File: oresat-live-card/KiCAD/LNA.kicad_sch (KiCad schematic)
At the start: 33 parts, among them J12 U.FL, J14 Conn_01x02, U18 TQP3M9037, U27 PAT1220-C-3DB, U28 PD2328J5050S2HF, U29 LTC5538

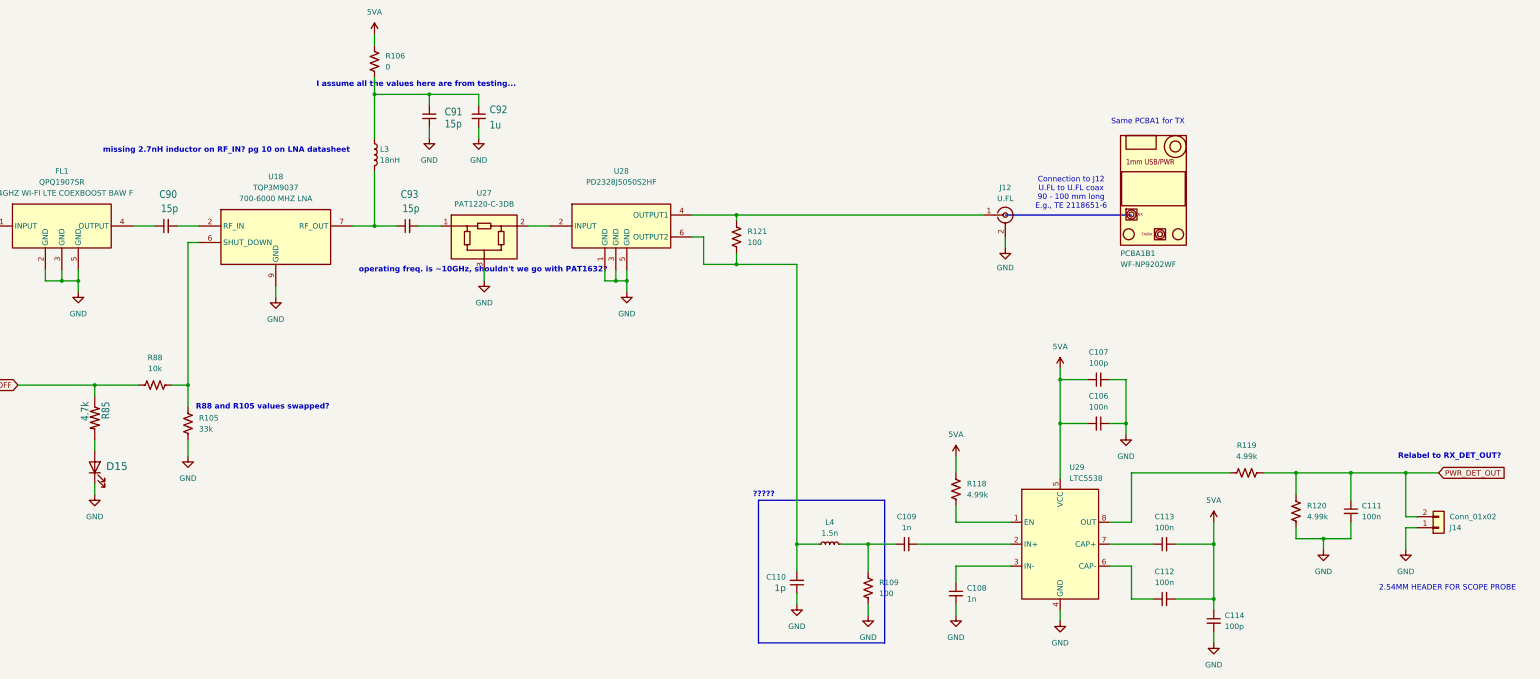
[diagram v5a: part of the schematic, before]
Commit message: swapped placement of R105 and R88, changed R109 from 100 to 56 ohms, relabelled PWR_DET_OUT to RX_DET_OUT, added inverter to TX/RX Control switch and swapped RF1 and RF2
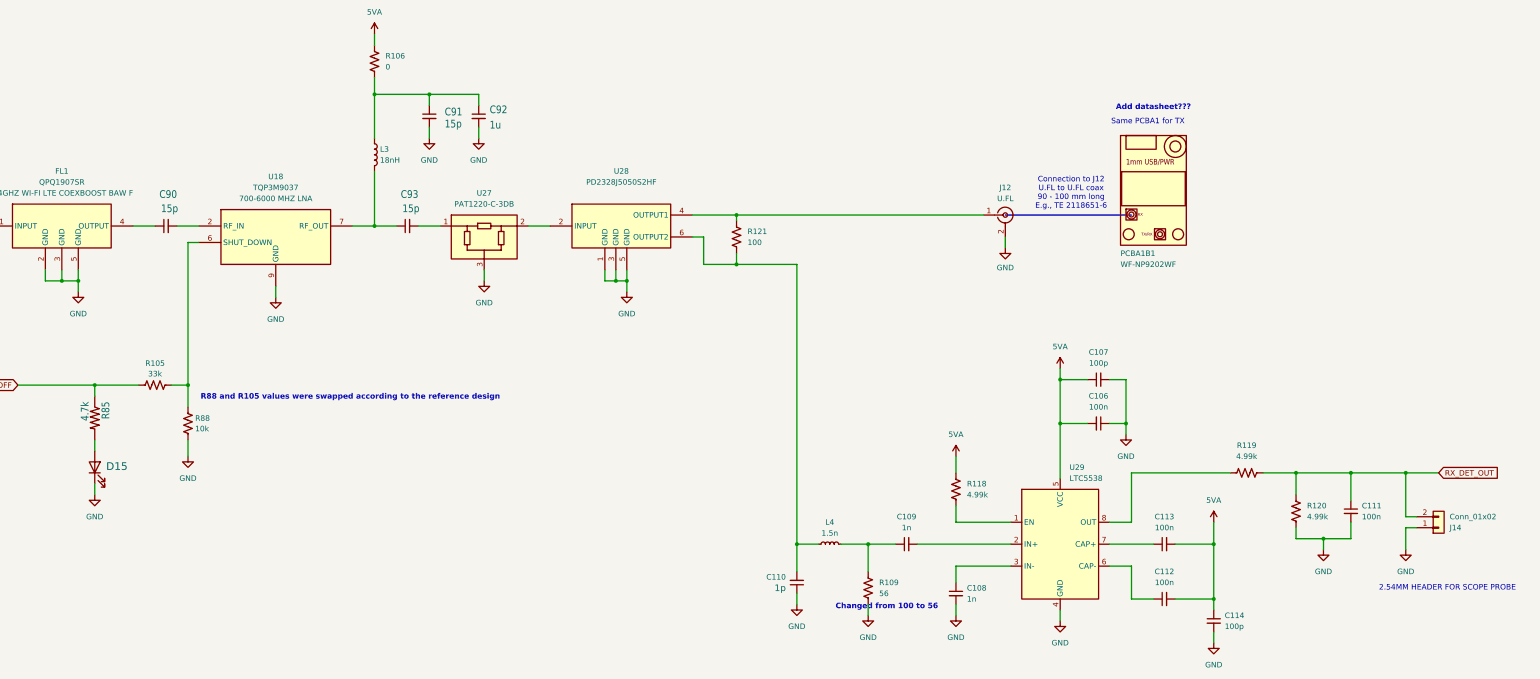
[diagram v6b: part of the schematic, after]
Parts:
- R109: value 100 -> 56
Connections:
- net GND: now also R88.2; no longer R105.2
- net PA_ON_LNA_OFF: now also R105.1; no longer R88.2
- net at R88.1, U18.6 (SHUT_DOWN): now also R105.2; no longer R105.1
- net PWR_DET_OUT renamed RX_DET_OUT
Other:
- note added: "Add datasheet???"
- note added: "Changed from 100 to 56"
- note added: "R88 and R105 values were swapped according to the reference design"
- note removed: "?????"
- note removed: "I assume all the values here are from testing..."
- note removed: "R88 and R105 values swapped?"
- note removed: "Relabel to RX_DET_OUT?"
- note removed: "missing 2.7nH inductor on RF_IN? pg 10 on LNA datasheet"
- note removed: "operating freq. is ~10GHz, shouldn't we go with PAT1632?"
- moved on the sheet: R105, R88
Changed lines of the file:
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@@
 		(rev "2")
 	)
-	(rectangle
-		(start 237.49 139.7)
-		(end 266.7 172.72)
-		(stroke
-			(width 0)
-			(type default)
-		)
-		(fill
-			(type none)
-		)
-	)
-	(text "I assume all the values here are from testing..."
-		(exclude_from_sim no)
-		(at 158.242 43.434 0)
-		(effects
-			(font
-				(size 1.27 1.27)
-				(thickness 0.254)
-				(bold yes)
-			)
-		)
-	)
 	(text "Same PCBA1 for TX"
 		(exclude_from_sim no)
@@
 		)
 	)
-	(text "missing 2.7nH inductor on RF_IN? pg 10 on LNA datasheet"
+	(text "Add datasheet??? "
 		(exclude_from_sim no)
-		(at 114.3 58.674 0)
-		(effects
-			(font
-				(size 1.27 1.27)
-				(thickness 0.254)
-				(bold yes)
-			)
-		)
-	)
-	(text "operating freq. is ~10GHz, shouldn't we go with PAT1632?"
-		(exclude_from_sim no)
-		(at 173.736 86.36 0)
+		(at 328.93 48.768 0)
 		(effects
 			(font
@@
 		)
 	)
-	(text "?????"
+	(text "Changed from 100 to 56"
 		(exclude_from_sim no)
-		(at 238.7267 138.3976 0)
+		(at 267.208 164.338 0)
 		(effects
 			(font
@@
 		)
 	)
-	(text "R88 and R105 values swapped?"
+	(text "R88 and R105 values were swapped according to the reference design"
 		(exclude_from_sim no)
-		(at 122.682 118.11 0)
-		(effects
-			(font
-				(size 1.27 1.27)
-				(thickness 0.254)
-				(bold yes)
-			)
-		)
-	)
-	(text "Relabel to RX_DET_OUT?"
-		(exclude_from_sim no)
-		(at 397.51 129.54 0)
+		(at 143.002 115.824 0)
 		(effects
 			(font
@@
 		)
 	)
-	(global_label "PWR_DET_OUT"
+	(global_label "RX_DET_OUT"
 		(shape input)
 		(at 394.97 133.35 0)
@@
 		)
 		(property "Intersheetrefs" "${INTERSHEET_REFS}"
-			(at 410.897 133.35 0)
+			(at 409.3851 133.35 0)
 			(effects
 				(font
@@
 			)
 		)
-		(property "Value" "100"
+		(property "Value" "56"
 			(at 265.43 161.2899 0)
 			(effects
@@
 	(symbol
 		(lib_id "Device:R_US")
-		(at 105.41 121.92 0)
+		(at 97.79 113.03 90)
 		(unit 1)
 		(exclude_from_sim no)
@@
 		(fields_autoplaced yes)
 		(property "Reference" "R105"
-			(at 107.95 120.6499 0)
+			(at 97.79 107.9965 90)
 			(effects
 				(font
 					(size 1.27 1.27)
 				)
-				(justify left)
 			)
 		)
 		(property "Value" "33k"
-			(at 107.95 123.1899 0)
+			(at 97.79 110.4208 90)
 			(effects
 				(font
 					(size 1.27 1.27)
 				)
-				(justify left)
 			)
 		)
 		(property "Footprint" "Resistor_SMD:R_0603_1608Metric"
-			(at 106.426 122.174 90)
+			(at 98.044 112.014 90)
 			(effects
 				(font
@@
 		)
 		(property "Datasheet" "~"
-			(at 105.41 121.92 0)
+			(at 97.79 113.03 0)
 			(effects
 				(font
@@
 		)
 		(property "Description" "RES 33K OHM 1% 1/10W 0603"
-			(at 105.41 121.92 0)
+			(at 97.79 113.03 0)
 			(effects
 				(font
@@
 		)
 		(property "DPN" "10-ERJ-U03F3302VCT-ND "
-			(at 105.41 121.92 0)
+			(at 97.79 113.03 0)
 			(effects
 				(font
@@
 		)
 		(property "Distributor" "DigiKey"
-			(at 105.41 121.92 0)
+			(at 97.79 113.03 0)
 			(effects
 				(font
@@
 		)
 		(property "MFR" "Panasonic "
-			(at 105.41 121.92 0)
+			(at 97.79 113.03 0)
 			(effects
 				(font
@@
 		)
 		(property "MPN" "ERJ-U03F3302V "
-			(at 105.41 121.92 0)
+			(at 97.79 113.03 0)
 			(effects
 				(font
@@
 	(symbol
 		(lib_id "Device:R_US")
-		(at 97.79 113.03 270)
+		(at 105.41 121.92 0)
 		(unit 1)
 		(exclude_from_sim no)
@@
 		(fields_autoplaced yes)
 		(property "Reference" "R88"
-			(at 97.79 106.68 90)
+			(at 107.061 120.7078 0)
 			(effects
 				(font
 					(size 1.27 1.27)
 				)
+				(justify left)
 			)
 		)
 		(property "Value" "10k"
-			(at 97.79 109.22 90)
+			(at 107.061 123.1321 0)
 			(effects
 				(font
 					(size 1.27 1.27)
 				)
+				(justify left)
 			)
 		)
 		(property "Footprint" "Resistor_SMD:R_0603_1608Metric"
-			(at 97.536 114.046 90)
+			(at 106.426 122.174 90)
 			(effects
 				(font
@@
 		)
 		(property "Datasheet" "~"
-			(at 97.79 113.03 0)
+			(at 105.41 121.92 0)
 			(effects
 				(font
@@
 		)
 		(property "Description" "RES SMD 10K OHM 1% 1/10W 0603"
-			(at 97.79 113.03 0)
+			(at 105.41 121.92 0)
 			(effects
 				(font
@@
 		)
 		(property "DPN" "P10.0KHCT-ND "
-			(at 97.79 113.03 90)
+			(at 105.41 121.92 90)
 			(effects
 				(font
@@
 		)
 		(property "Distributor" "DigiKey"
-			(at 97.79 113.03 90)
+			(at 105.41 121.92 90)
 			(effects
 				(font
@@
 		)
 		(property "MFR" "Panasonic "
-			(at 97.79 113.03 90)
+			(at 105.41 121.92 90)
 			(effects
 				(font
@@
 		)
 		(property "MPN" "ERJ-3EKF1002V"
-			(at 97.79 113.03 90)
+			(at 105.41 121.92 90)
 			(effects
 				(font

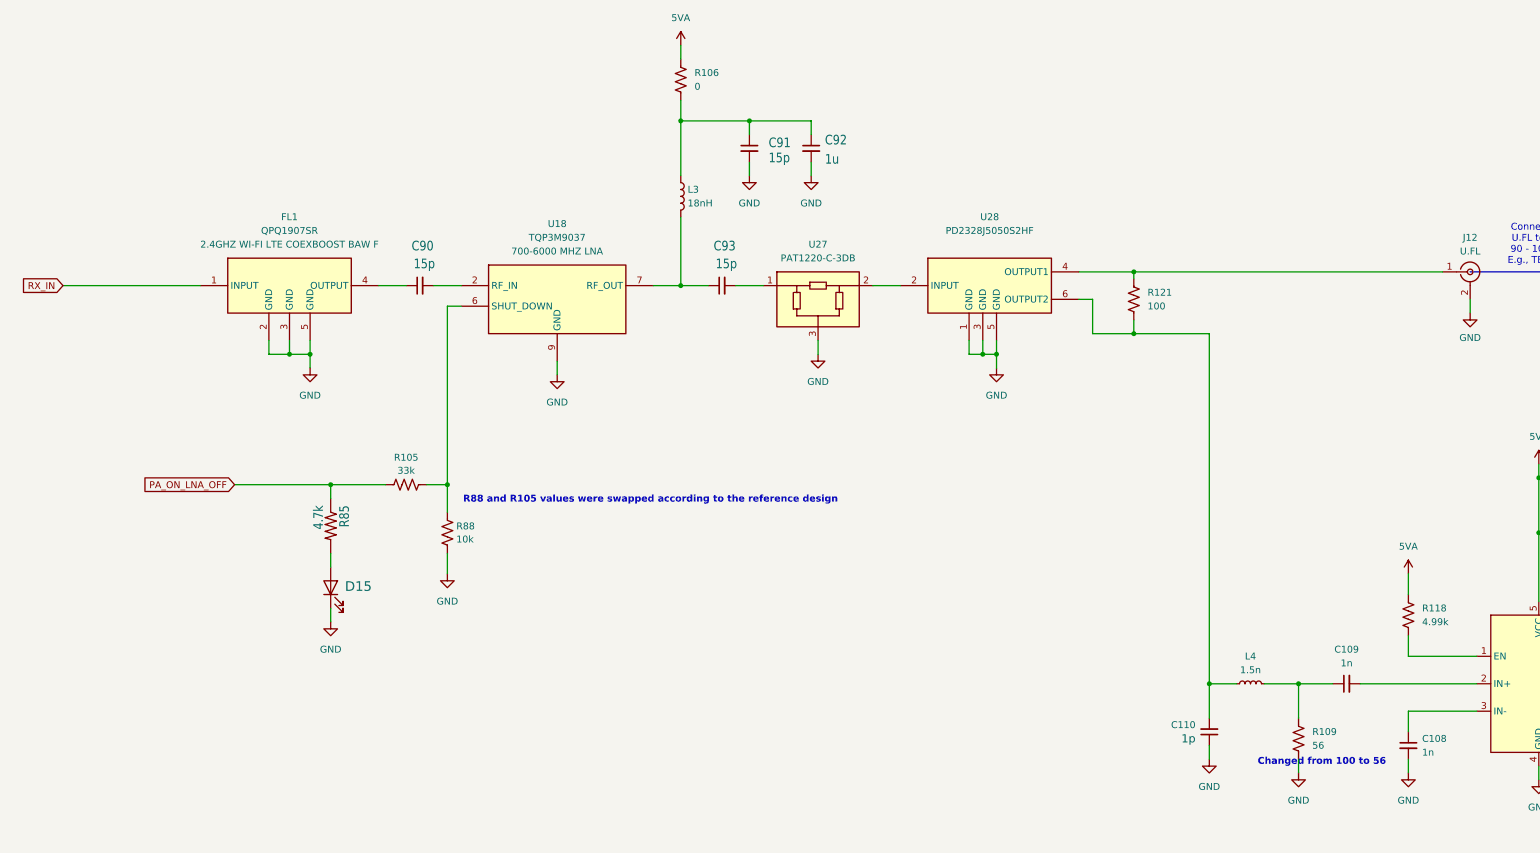
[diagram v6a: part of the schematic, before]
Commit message: Added extra filter to RX_IN on LNA side, continued routing
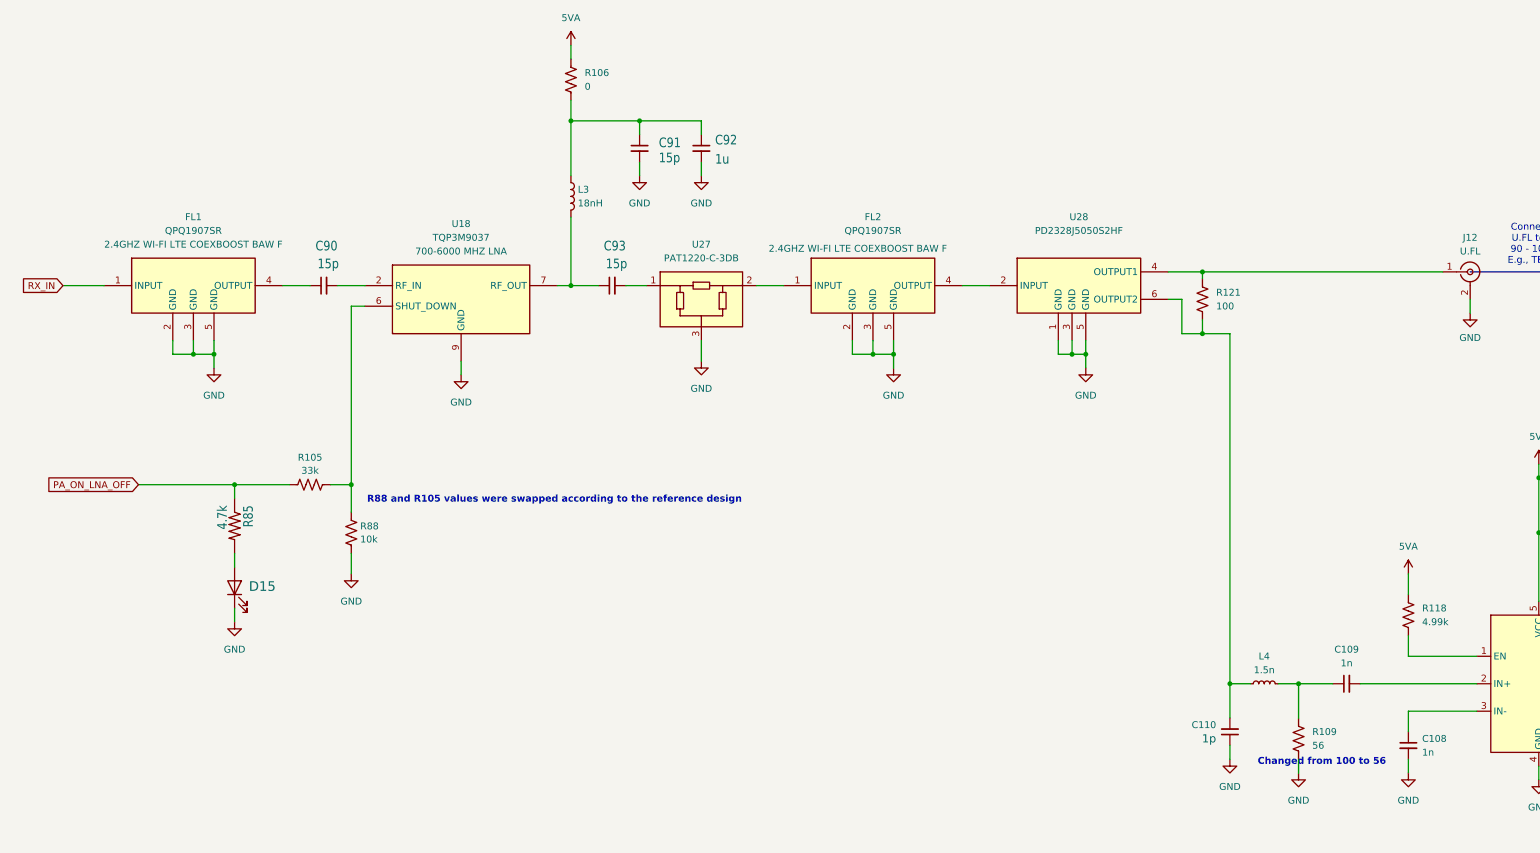
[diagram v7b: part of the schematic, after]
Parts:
- added FL2: QPQ1907SR, oresat-ics:QPQ1907SR, symbol oresat-ics:QPQ1907SR_2.4GHz_BPF
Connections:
- net GND: now also FL2.2 (GND), FL2.3 (GND), FL2.5 (GND)
- net at U27.2: now also FL2.1 (INPUT); no longer U28.2 (INPUT)
- new net: FL2.4 (OUTPUT), U28.2 (INPUT)
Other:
- moved on the sheet: C110, C90, C91, C92, C93, D15, FL1, L3, L4, R105, R106, R121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

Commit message: initial routing pass completed, moved R144 and R155 to output of U6.
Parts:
- C91: footprint oresat-passives:0402-C-NOSILK -> Capacitor_SMD:C_0402_1005Metric
- C92, R106: footprint Resistor_SMD:R_0603_1608Metric -> Capacitor_SMD:C_0402_1005Metric
- U28: footprint oresat-misc:PD2328J5050S2HF -> PD2328J5050S2HF
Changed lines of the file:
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@@
 			)
 		)
-		(property "Footprint" "oresat-passives:0402-C-NOSILK"
+		(property "Footprint" "Capacitor_SMD:C_0402_1005Metric"
 			(at 140.97 50.8 0)
 			(effects
@@
 			)
 		)
-		(property "Footprint" "oresat-misc:PD2328J5050S2HF"
+		(property "Footprint" "PD2328J5050S2HF"
 			(at 234.95 168.58 0)
 			(effects
@@
 			)
 		)
-		(property "Footprint" "Resistor_SMD:R_0603_1608Metric"
+		(property "Footprint" "Capacitor_SMD:C_0402_1005Metric"
 			(at 152.4 50.8 0)
 			(effects
@@
 			)
 		)
-		(property "Footprint" "Resistor_SMD:R_0603_1608Metric"
+		(property "Footprint" "Capacitor_SMD:C_0402_1005Metric"
 			(at 127.254 37.846 90)
 			(effects
